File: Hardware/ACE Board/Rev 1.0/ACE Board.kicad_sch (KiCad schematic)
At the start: 187 parts, among them J1 PHI2 SELECT, J10 PORT A, J11 AUDIO L, J12 DB9 MALE (DTE), J13 PS/2, J14 AUDIO R, J15 AUDIO, J16 5V DC, J17 CART, J18 BUS, J19 VCC, J2 CTS EN, J20 POWER LED, J21 STORAGE, J22 KEYBOARD, J3 RESET SW, J4 DCD EN, J5 VDD, J6 JOYSTICK A, J7 PADDLES, J8 JOYSTICK B, J9 PORT B, SW1 `, SW10 9, SW11 0, SW12 -, SW13 =, SW14 BACKSPACE, SW15 ESCAPE, SW16 TAB, SW17 Q, SW18 W, SW19 E, SW2 1, SW20 R, SW21 T, SW22 Y, SW23 U, SW24 I, SW25 O, SW26 P, SW27 [, SW28 ], SW29 \, SW3 2, SW30 INSERT, SW31 CAPS LOCK, SW32 A, SW33 S, SW34 D, SW35 F, SW36 G, SW37 H, SW38 J, SW39 K, SW4 3, SW40 L, SW41 SHIFT, SW42 ;, SW43 ', SW44 ENTER, SW45 DELETE, SW46 Z, SW47 X, SW48 C, SW49 SHIFT, SW5 4, SW50 V, SW51 B, SW52 N, SW53 M, SW54 ,, SW55 ., SW56 /, SW57 UP ARROW, SW58 CTRL, SW59 ALT, SW6 5, SW60 MENU, SW61 SPACE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

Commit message: Update BOM
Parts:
- J13: Mouser (none) -> 806-KMDGX-6S-BS
- U20: Mouser (none) -> 595-SN74HC138N
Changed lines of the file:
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@@
 			)
 		)
+		(property "Mouser" "595-SN74HC138N"
+			(at 123.19 344.17 0)
+			(hide yes)
+			(show_name no)
+			(do_not_autoplace no)
+			(effects
+				(font
+					(size 1.27 1.27)
+				)
+			)
+		)
 		(pin "14"
 		)
@@
 			(at 196.85 187.96 0)
 			(hide yes)
+			(show_name no)
+			(do_not_autoplace no)
+			(effects
+				(font
+					(size 1.27 1.27)
+				)
+			)
+		)
+		(property "Mouser" "806-KMDGX-6S-BS"
+			(at 196.85 187.96 0)
+			(hide yes)

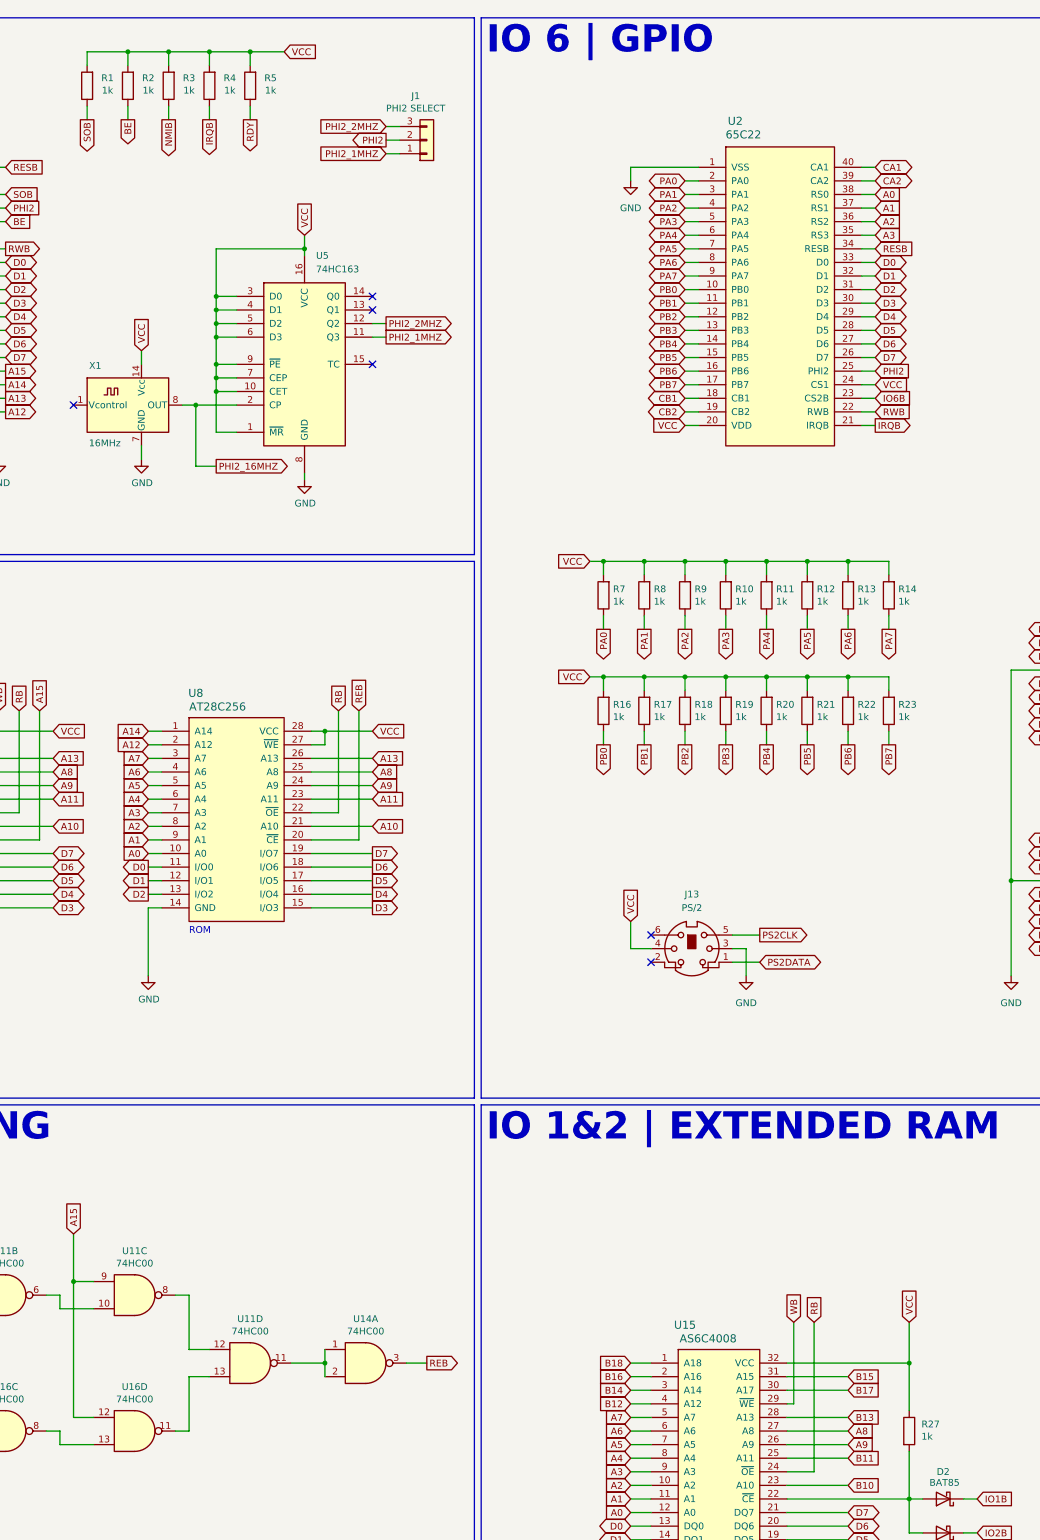
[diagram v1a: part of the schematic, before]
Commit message: Change some pullup resistor values
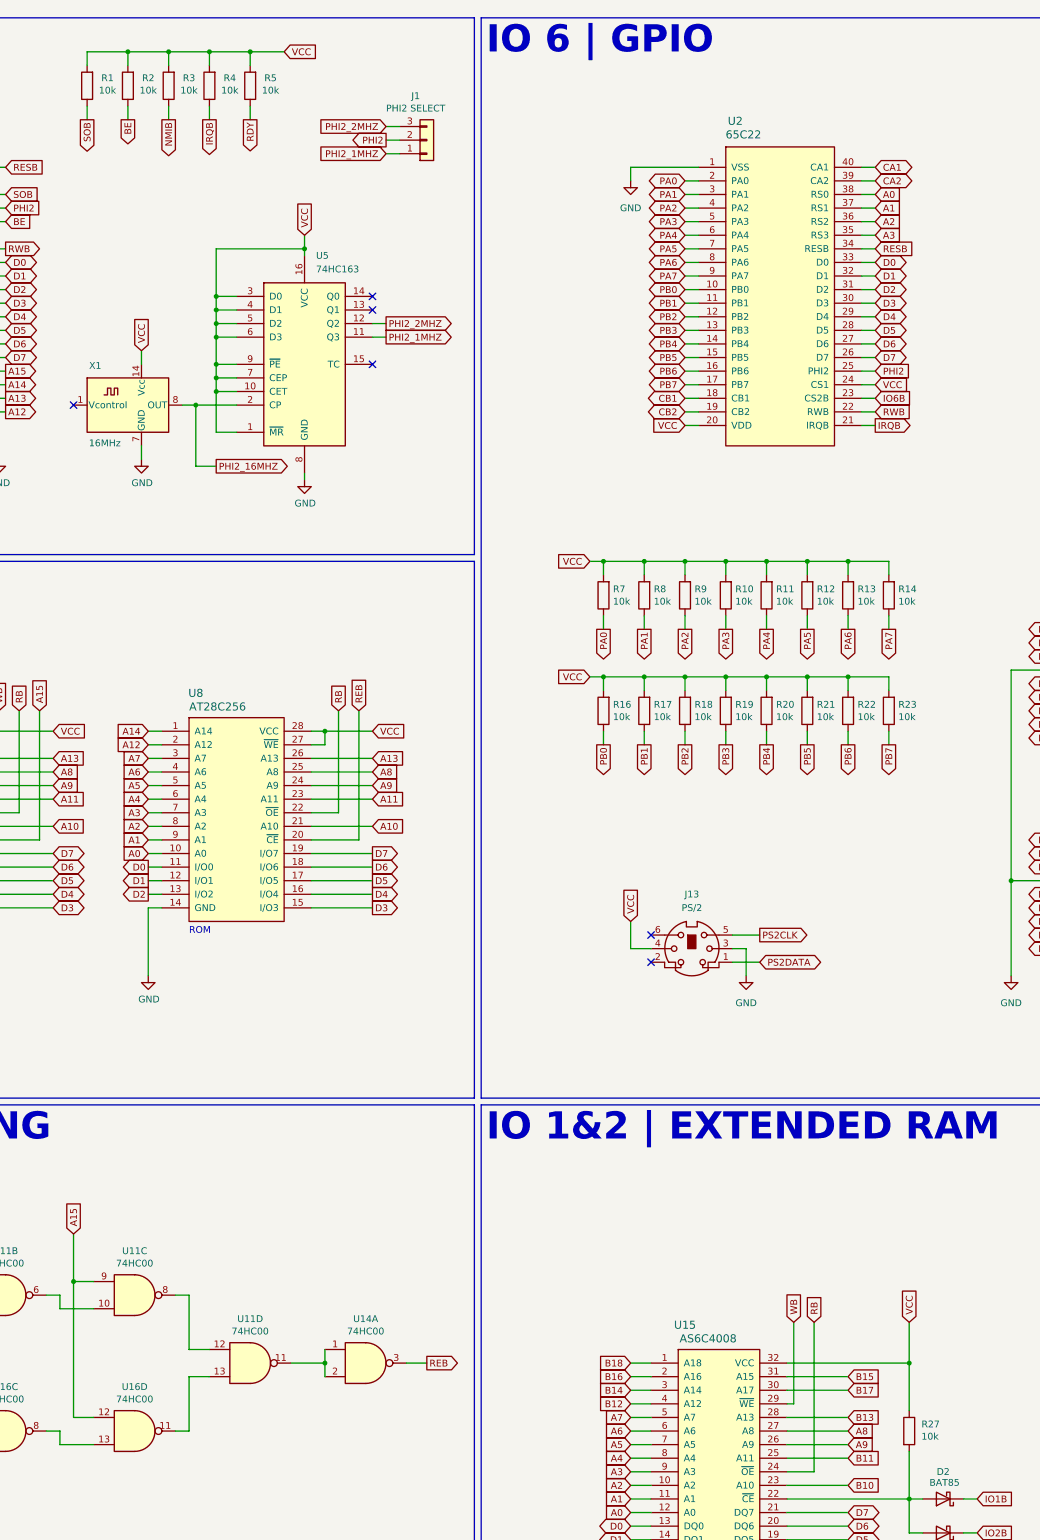
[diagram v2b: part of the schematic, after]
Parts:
- R1, R10, R11, R12, R13, R14, R16, R17, R18, R19, R2, R20, R21, R22, R23, R27, R3, R4, R5, R7, R8, R9: value 1k -> 10k
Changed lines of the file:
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@@
 			)
 		)
-		(property "Value" "1k"
+		(property "Value" "10k"
 			(at 110.49 27.5336 0)
 			(show_name no)
@@
 			)
 		)
-		(property "Value" "1k"
+		(property "Value" "10k"
 			(at 102.87 27.5336 0)
 			(show_name no)
@@
 			)
 		)
-		(property "Value" "1k"
+		(property "Value" "10k"
 			(at 235.458 123.063 0)
 			(show_name no)
@@
 			)
 		)
-		(property "Value" "1k"
+		(property "Value" "10k"
 			(at 182.118 144.653 0)
 			(show_name no)
@@
 			)
 		)
-		(property "Value" "1k"
+		(property "Value" "10k"
 			(at 204.978 144.653 0)
 			(show_name no)
@@
 			)
 		)
-		(property "Value" "1k"
+		(property "Value" "10k"
 			(at 220.218 144.653 0)
 			(show_name no)
@@
 			)
 		)
-		(property "Value" "1k"
+		(property "Value" "10k"
 			(at 95.25 27.5336 0)
 			(show_name no)
@@
 			)
 		)
-		(property "Value" "1k"
+		(property "Value" "10k"
 			(at 189.738 144.653 0)
 			(show_name no)
@@
 			)
 		)
-		(property "Value" "1k"
+		(property "Value" "10k"
 			(at 182.118 123.063 0)
 			(show_name no)
@@
 			)
 		)
-		(property "Value" "1k"
+		(property "Value" "10k"
 			(at 220.218 123.063 0)
 			(show_name no)
@@
 			)
 		)
-		(property "Value" "1k"
+		(property "Value" "10k"
 			(at 197.358 144.653 0)
 			(show_name no)
@@
 			)
 		)
-		(property "Value" "1k"
+		(property "Value" "10k"
 			(at 189.738 123.063 0)
 			(show_name no)
@@
 			)
 		)
-		(property "Value" "1k"
+		(property "Value" "10k"
 			(at 204.978 123.063 0)
 			(show_name no)
@@
 			)
 		)
-		(property "Value" "1k"
+		(property "Value" "10k"
 			(at 87.63 27.5336 0)
 			(show_name no)
@@
 			)
 		)
-		(property "Value" "1k"
+		(property "Value" "10k"
 			(at 197.358 123.063 0)
 			(show_name no)
@@
 			)
 		)
-		(property "Value" "1k"
+		(property "Value" "10k"
 			(at 118.11 27.5336 0)
 			(show_name no)
@@
 			)
 		)
-		(property "Value" "1k"
+		(property "Value" "10k"
 			(at 235.458 144.653 0)
 			(show_name no)
@@
 			)
 		)
-		(property "Value" "1k"
+		(property "Value" "10k"
 			(at 212.598 123.063 0)
 			(show_name no)
@@
 			)
 		)
-		(property "Value" "1k"
+		(property "Value" "10k"
 			(at 239.776 279.146 0)
 			(show_name no)
@@
 			)
 		)
-		(property "Value" "1k"
+		(property "Value" "10k"
 			(at 227.838 123.063 0)
 			(show_name no)
@@
 			)
 		)
-		(property "Value" "1k"
+		(property "Value" "10k"
 			(at 227.838 144.653 0)
 			(show_name no)
@@
 			)
 		)
-		(property "Value" "1k"
+		(property "Value" "10k"
 			(at 212.598 144.653 0)
 			(show_name no)

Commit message: Change some pullup resistor values
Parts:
- removed R1: 10k, Resistor_THT:R_Axial_DIN0204_L3.6mm_D1.6mm_P5.08mm_Horizontal, symbol Device:R
- R10: renamed from R11; value 10k -> 1k
- R11: renamed from R12; value 10k -> 1k
- R12: renamed from R13; value 10k -> 1k
- R13: renamed from R14; value 10k -> 1k
- R14: renamed from R16; value 10k -> 1k
- R15: renamed from R17; value 10k -> 1k
- R16: renamed from R18; value 10k -> 1k
- R17: renamed from R19; value 10k -> 1k
- R18: renamed from R20; value 10k -> 1k
- R19: renamed from R21; value 10k -> 1k
- R20: renamed from R22; value 10k -> 1k
- R21: renamed from R23; value 10k -> 1k
- R6: renamed from R7; value 10k -> 1k
- R7: renamed from R8; value 10k -> 1k
- R8: renamed from R9; value 10k -> 1k
- R9: renamed from R10; value 10k -> 1k
- renumbered J22 to J14, J14 to J15, J15 to J16, J16 to J17, J17 to J18, J18 to J19, J19 to J20, J20 to J21, J21 to J22, R2 to R1, R3 to R2, R24 to R22, R25 to R23, R26 to R24, R27 to R25, R28 to R26, R29 to R27, R30 to R28, R31 to R29, R4 to R3, R32 to R30, R33 to R31, R34 to R32, R35 to R33, R36 to R34, R5 to R4, R6 to R5, SW70 to SW17, SW17 to SW18, SW18 to SW19, SW19 to SW20, SW20 to SW21, SW21 to SW22, SW22 to SW23, SW23 to SW24, SW24 to SW25, SW25 to SW26, SW26 to SW27, SW27 to SW28, SW28 to SW29, SW29 to SW30, SW30 to SW31, SW31 to SW32, SW32 to SW33, SW33 to SW34, SW34 to SW35, SW35 to SW36, SW36 to SW37, SW37 to SW38, SW38 to SW39, SW39 to SW40, SW40 to SW41, SW41 to SW42, SW42 to SW43, SW43 to SW44, SW44 to SW45, SW45 to SW46, SW46 to SW47, SW47 to SW48, SW48 to SW49, SW49 to SW50, SW50 to SW51, SW51 to SW52, SW52 to SW53, SW53 to SW54, SW54 to SW55, SW55 to SW56, SW56 to SW57, SW57 to SW58, SW58 to SW59, SW59 to SW60, SW60 to SW61, SW61 to SW62, SW62 to SW63, SW63 to SW64, SW64 to SW65, SW65 to SW66, SW66 to SW67, SW67 to SW68, SW68 to SW69, SW69 to SW70
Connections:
- net SOB is gone; now on net VCC: U1.38 (SOB)
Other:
- moved on the sheet: R1, R2, R3, R4

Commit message: Ensure accurate Rev 1.0
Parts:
- R1, R2, R25, R3, R4: value 10k -> 1k
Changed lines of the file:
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@@
 			)
 		)
-		(property "Value" "10k"
+		(property "Value" "1k"
 			(at 105.41 27.5336 0)
 			(show_name no)
@@
 			)
 		)
-		(property "Value" "10k"
+		(property "Value" "1k"
 			(at 97.79 27.5336 0)
 			(show_name no)
@@
 			)
 		)
-		(property "Value" "10k"
+		(property "Value" "1k"
 			(at 90.17 27.5336 0)
 			(show_name no)
@@
 			)
 		)
-		(property "Value" "10k"
+		(property "Value" "1k"
 			(at 113.03 27.5336 0)
 			(show_name no)
@@
 			)
 		)
-		(property "Value" "10k"
+		(property "Value" "1k"
 			(at 239.776 279.146 0)
 			(show_name no)
